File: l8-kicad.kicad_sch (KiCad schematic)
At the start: 5 parts, among them J3 Screw_Terminal_01x06

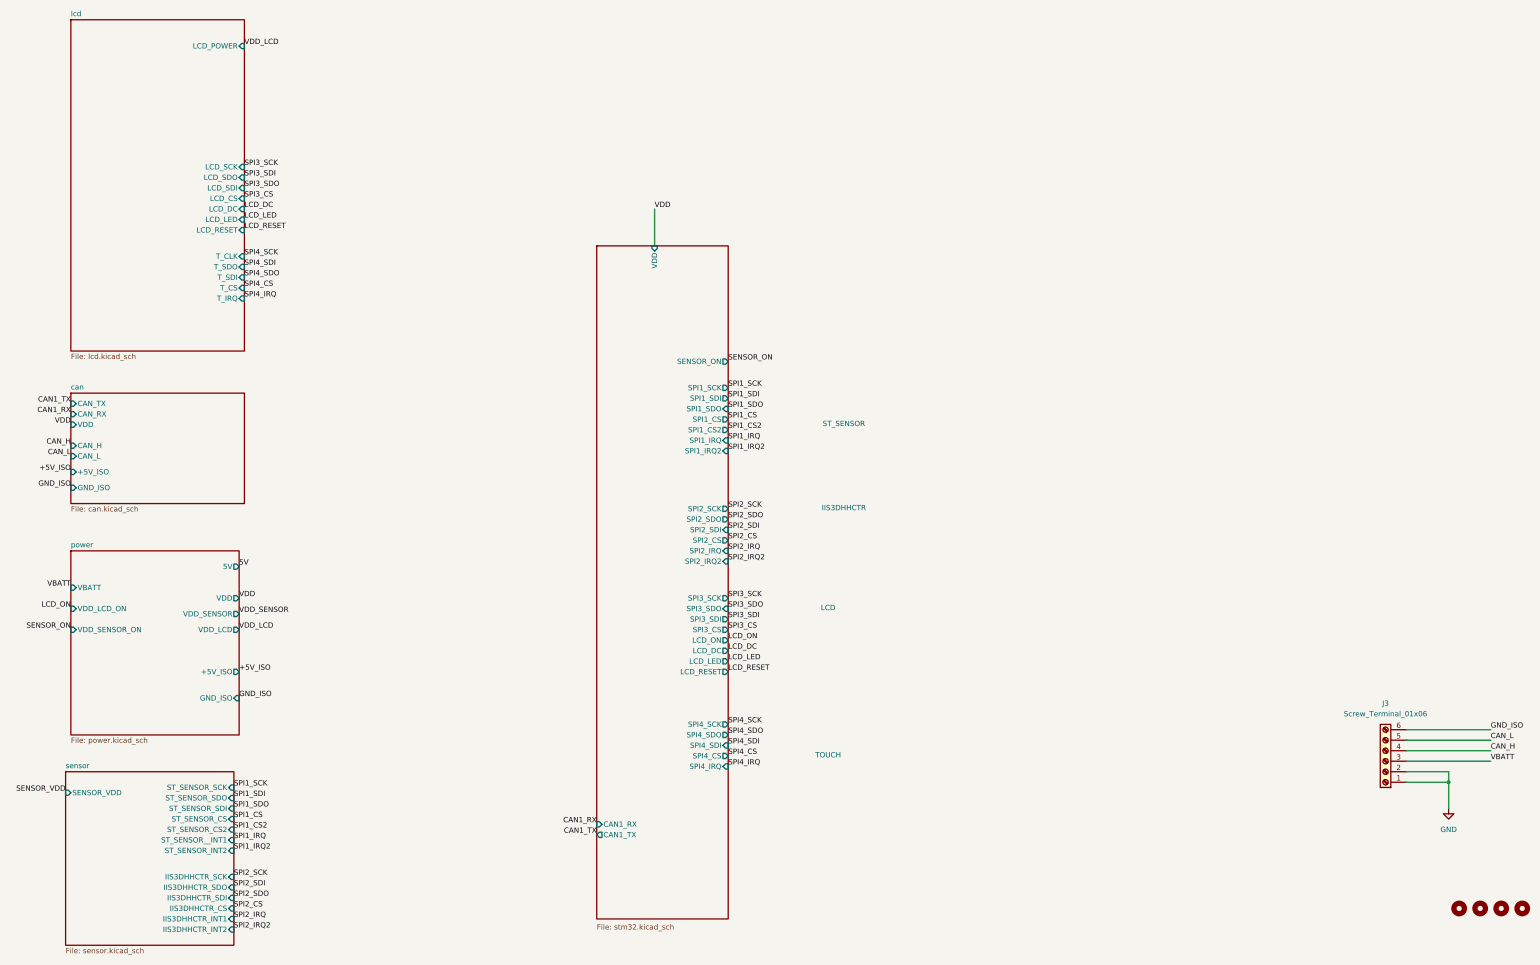
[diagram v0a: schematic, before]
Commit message: change power add buzzer
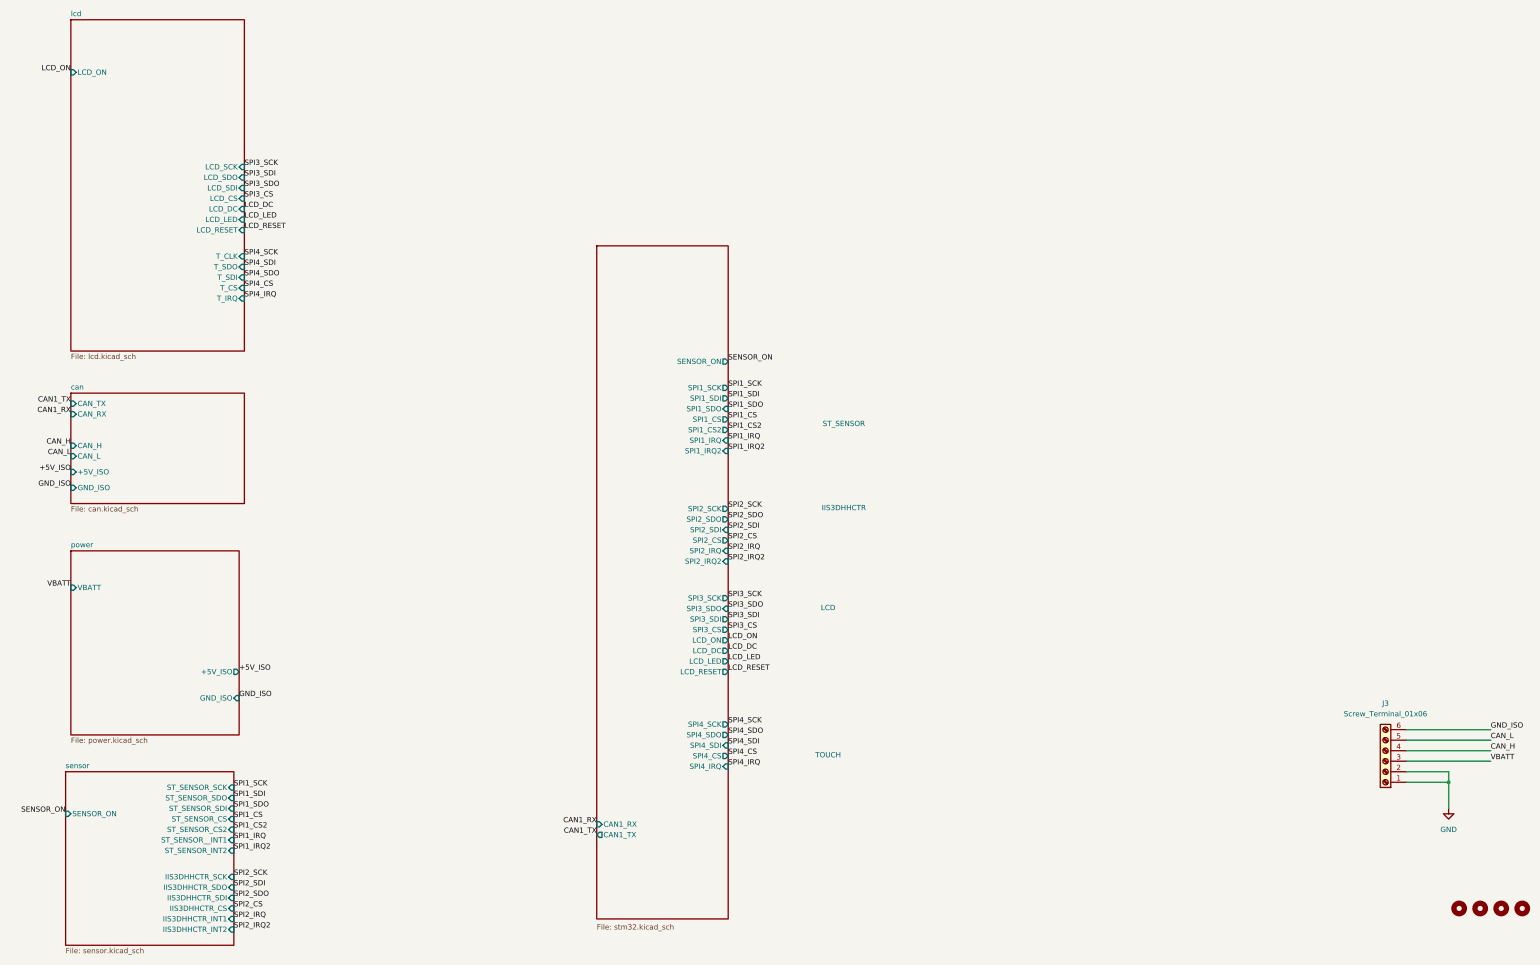
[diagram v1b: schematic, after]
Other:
- sheet MCU ports: added none; removed VDD
- sheet can ports: added none; removed VDD
- sheet lcd ports: added LCD_ON; removed LCD_POWER
- sheet power ports: added none; removed 5V, VDD, VDD_LCD, VDD_LCD_ON, VDD_SENSOR, VDD_SENSOR_ON
- sheet sensor ports: added SENSOR_ON; removed SENSOR_VDD
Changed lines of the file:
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@@
 	(wire
 		(pts
-			(xy 194.31 76.2) (xy 194.31 85.09)
+			(xy 375.92 201.93) (xy 396.24 201.93)
 		)
 		(stroke
@@
 	(wire
 		(pts
-			(xy 375.92 201.93) (xy 396.24 201.93)
+			(xy 386.08 214.63) (xy 386.08 220.98)
 		)
 		(stroke
@@
 	(wire
 		(pts
-			(xy 386.08 214.63) (xy 386.08 220.98)
+			(xy 375.92 207.01) (xy 396.24 207.01)
 		)
 		(stroke
@@
 		)
 	)
-	(wire
-		(pts
-			(xy 375.92 207.01) (xy 396.24 207.01)
-		)
-		(stroke
-			(width 0)
-			(type default)
-		)
-	)
 	(text "ST_SENSOR"
 		(exclude_from_sim no)
@@
 		)
 	)
-	(label "SENSOR_ON"
-		(at 53.34 177.8 180)
-		(fields_autoplaced yes)
-		(effects
-			(font
-				(size 1.27 1.27)
-			)
-			(justify right bottom)
-		)
-	)
 	(label "SPI1_IRQ"
 		(at 92.71 228.6 0)
@@
 		)
 	)
-	(label "VDD_LCD"
-		(at 93.98 177.8 0)
-		(fields_autoplaced yes)
-		(effects
-			(font
-				(size 1.27 1.27)
-			)
-			(justify left bottom)
-		)
-	)
 	(label "SPI4_SDI"
 		(at 212.09 205.74 0)
@@
 		)
 	)
-	(label "VDD"
-		(at 194.31 76.2 0)
-		(fields_autoplaced yes)
-		(effects
-			(font
-				(size 1.27 1.27)
-			)
-			(justify left bottom)
-		)
-	)
 	(label "SPI2_IRQ"
 		(at 92.71 247.65 0)
@@
 		)
 	)
-	(label "5V"
-		(at 93.98 162.56 0)
-		(fields_autoplaced yes)
-		(effects
-			(font
-				(size 1.27 1.27)
-			)
-			(justify left bottom)
-		)
-	)
 	(label "SPI3_SDO"
 		(at 212.09 172.72 0)
@@
 		)
 	)
-	(label "VDD_LCD"
-		(at 95.25 36.83 0)
-		(fields_autoplaced yes)
-		(effects
-			(font
-				(size 1.27 1.27)
-			)
-			(justify left bottom)
-		)
-	)
 	(label "LCD_RESET"
 		(at 95.25 81.28 0)
@@
 		)
 	)
-	(label "VDD"
-		(at 53.34 128.27 180)
-		(fields_autoplaced yes)
-		(effects
-			(font
-				(size 1.27 1.27)
-			)
-			(justify right bottom)
-		)
-	)
 	(label "SPI4_IRQ"
 		(at 212.09 210.82 0)
@@
 		)
 	)
-	(label "VDD"
-		(at 93.98 170.18 0)
-		(fields_autoplaced yes)
-		(effects
-			(font
-				(size 1.27 1.27)
-			)
-			(justify left bottom)
+	(label "LCD_ON"
+		(at 53.34 43.18 180)
+		(effects
+			(font
+				(size 1.27 1.27)
+			)
+			(justify right bottom)
 		)
 	)
@@
 		)
 	)
-	(label "VDD_SENSOR"
-		(at 93.98 173.99 0)
-		(fields_autoplaced yes)
-		(effects
-			(font
-				(size 1.27 1.27)
-			)
-			(justify left bottom)
-		)
-	)
 	(label "VBATT"
 		(at 53.34 167.64 180)
@@
 		)
 	)
-	(label "SENSOR_VDD"
-		(at 52.07 217.17 180)
-		(fields_autoplaced yes)
-		(effects
-			(font
-				(size 1.27 1.27)
-			)
-			(justify right bottom)
-		)
-	)
 	(label "SPI2_IRQ2"
 		(at 92.71 250.19 0)
@@
 		)
 	)
-	(label "LCD_ON"
-		(at 53.34 172.72 180)
-		(fields_autoplaced yes)
+	(label "SENSOR_ON"
+		(at 52.07 222.25 180)
 		(effects
 			(font
@@
 			)
 		)
-		(pin "VDD" input
-			(at 194.31 85.09 90)
-			(effects
-				(font
-					(size 1.27 1.27)
-				)
-				(justify right)
-			)
-		)
 		(pin "SPI1_SCK" output
 			(at 212.09 119.38 0)
@@
 			)
 		)
-		(pin "VDD" input
-			(at 53.34 128.27 180)
-			(effects
-				(font
-					(size 1.27 1.27)
-				)
-				(justify left)
-			)
-		)
 		(pin "GND_ISO" input
 			(at 53.34 143.51 180)
@@
 			)
 		)
-		(pin "SENSOR_VDD" input
-			(at 52.07 217.17 180)
-			(effects
-				(font
-					(size 1.27 1.27)
-				)
-				(justify left)
-			)
-		)
 		(pin "IIS3DHHCTR_SDO" input
 			(at 92.71 240.03 0)
@@
 				)
 				(justify right)
+			)
+		)
+		(pin "SENSOR_ON" input
+			(at 52.07 222.25 180)
+			(effects
+				(font
+					(size 1.27 1.27)
+				)
+				(justify left)
 			)
 		)
@@
 			)
 		)
-		(pin "LCD_POWER" input
-			(at 95.25 36.83 0)
-			(effects
-				(font
-					(size 1.27 1.27)
-				)
-				(justify right)
+		(pin "LCD_ON" input
+			(at 53.34 43.18 180)
+			(effects
+				(font
+					(size 1.27 1.27)
+				)
+				(justify left)
 			)
 		)
@@
 			)
 		)
-		(pin "VDD" output
-			(at 93.98 170.18 0)
-			(effects
-				(font
-					(size 1.27 1.27)
-				)
-				(justify right)
-			)
-		)
-		(pin "5V" output
-			(at 93.98 162.56 0)
-			(effects
-				(font
-					(size 1.27 1.27)
-				)
-				(justify right)
-			)
-		)
 		(pin "VBATT" input
 			(at 53.34 167.64 180)
@@
 			)
 		)
-		(pin "VDD_LCD_ON" input
-			(at 53.34 172.72 180)
-			(effects
-				(font
-					(size 1.27 1.27)
-				)
-				(justify left)
-			)
-		)
-		(pin "VDD_SENSOR_ON" input
-			(at 53.34 177.8 180)
-			(effects
-				(font
-					(size 1.27 1.27)
-				)
-				(justify left)
-			)
-		)
-		(pin "VDD_SENSOR" output
-			(at 93.98 173.99 0)
-			(effects
-				(font
-					(size 1.27 1.27)
-				)
-				(justify right)
-			)
-		)
-		(pin "VDD_LCD" output
-			(at 93.98 177.8 0)
-			(effects
-				(font
-					(size 1.27 1.27)
-				)
-				(justify right)
-			)
-		)

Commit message: usb sheet
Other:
- added sheet usb (usb.kicad_sch)
- sheet MCU ports: added PA10, USB_OTG_FS_DM, USB_OTG_FS_DP, USB_OTG_FS_VBUS; removed none
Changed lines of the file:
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@@
+		)
+	)
+	(label "USB_OTG_FS_DP"
+		(at 180.34 91.44 180)
+		(effects
+			(font
+				(size 1.27 1.27)
+			)
+			(justify right bottom)
+		)
+	)
+	(label "USB_OTG_FS_VBUS"
+		(at 349.25 74.93 0)
+		(effects
+			(font
+				(size 1.27 1.27)
+			)
+			(justify left bottom)
 		)
 	)
@@
 		)
 	)
+	(label "USB_OTG_FS_DP"
+		(at 349.25 59.69 0)
+		(effects
+			(font
+				(size 1.27 1.27)
+			)
+			(justify left bottom)
+		)
+	)
 	(label "LCD_DC"
 		(at 212.09 182.88 0)
@@
 		)
 	)
+	(label "USB_OTG_FS_VBUS"
+		(at 180.34 104.14 180)
+		(effects
+			(font
+				(size 1.27 1.27)
+			)
+			(justify right bottom)
+		)
+	)
+	(label "USB_OTG_FS_DM"
+		(at 349.25 64.77 0)
+		(effects
+			(font
+				(size 1.27 1.27)
+			)
+			(justify left bottom)
+		)
+	)
 	(label "LCD_LED"
 		(at 212.09 185.42 0)
@@
 		)
 	)
+	(label "USB_OTG_FS_DM"
+		(at 180.34 99.06 180)
+		(effects
+			(font
+				(size 1.27 1.27)
+			)
+			(justify right bottom)
+		)
+	)
 	(label "CAN_H"
 		(at 53.34 133.35 180)
@@
 		)
 	)
+	(label "PA10"
+		(at 349.25 69.85 0)
+		(effects
+			(font
+				(size 1.27 1.27)
+			)
+			(justify left bottom)
+		)
+	)
 	(label "SPI1_SCK"
 		(at 212.09 119.38 0)
@@
 			)
 			(justify left bottom)
+		)
+	)
+	(label "PA10"
+		(at 180.34 95.25 180)
+		(effects
+			(font
+				(size 1.27 1.27)
+			)
+			(justify right bottom)
 		)
 	)
@@
 			)
 		)
+		(pin "USB_OTG_FS_DP" bidirectional
+			(at 180.34 91.44 180)
+			(effects
+				(font
+					(size 1.27 1.27)
+				)
+				(justify left)
+			)
+		)
+		(pin "PA10" bidirectional
+			(at 180.34 95.25 180)
+			(effects
+				(font
+					(size 1.27 1.27)
+				)
+				(justify left)
+			)
+		)
+		(pin "USB_OTG_FS_DM" bidirectional
+			(at 180.34 99.06 180)
+			(effects
+				(font
+					(size 1.27 1.27)
+				)
+				(justify left)
+			)
+		)
+		(pin "USB_OTG_FS_VBUS" input
+			(at 180.34 104.14 180)
+			(effects
+				(font
+					(size 1.27 1.27)
+				)
+				(justify left)
+			)
+		)
 		(instances
 			(project "l8-kicad"
@@
 				)
 			)
+		)
+	)
+	(sheet
+		(at 298.45 48.26)
+		(size 50.8 58.42)
+		(fields_autoplaced yes)
+		(stroke
+			(width 0.1524)
+			(type solid)
+		)
+		(fill
+			(color 0 0 0 0.0000)
+		)
+		(property "Sheetname" "usb"
+			(at 298.45 47.5484 0)
+			(effects
+				(font
+					(size 1.27 1.27)
+				)
+				(justify left bottom)
+			)
+		)
+		(property "Sheetfile" "usb.kicad_sch"
+			(at 298.45 107.2646 0)
+			(effects
+				(font
+					(size 1.27 1.27)
+				)
+				(justify left top)
+			)
+		)
+		(pin "USB_OTG_FS_DP" bidirectional
+			(at 349.25 59.69 0)
+			(effects
+				(font
+					(size 1.27 1.27)
+				)
+				(justify right)
+			)
+		)
+		(pin "USB_OTG_FS_DM" bidirectional
+			(at 349.25 64.77 0)
+			(effects
+				(font
+					(size 1.27 1.27)
+				)
+				(justify right)
+			)
+		)
+		(pin "PA10" bidirectional
+			(at 349.25 69.85 0)
+			(effects
+				(font
+					(size 1.27 1.27)
+				)
+				(justify right)
+			)
+		)
+		(pin "USB_OTG_FS_VBUS" output
+			(at 349.25 74.93 0)
+			(effects
+				(font
+					(size 1.27 1.27)
+				)
+				(justify right)
+			)
+		)
+		(instances
+			(project "l8-kicad"
+				(path "/8d063f79-9282-4820-bcf4-1ff3c006cf08"
+					(page "7")
+				)
+			)
